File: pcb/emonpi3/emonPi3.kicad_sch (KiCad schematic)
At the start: 130 parts, among them CN1 CONN_03SCREW, CN2 CONN_03SCREW, CN3 CONN_03SCREW, J10 Conn_ARM_JTAG_SWD_10, J11 Conn_02x13_Odd_Even, J12 PINHD-1X9, J7 CONN_04PTH, J8 CONN_04PTH, J9 USB_C_Receptacle_USB2.0, SW1 SW_Push, SW2 SW_Push, SW3 SW_Push, U1 MCP1501-10xCH, U2 USBLC6-2P6, U3 ATSAMD21J17A-M, U4 AP2112K-3.3, U6 LMV331, U7 RFM69CW, U8 24AA02-OT

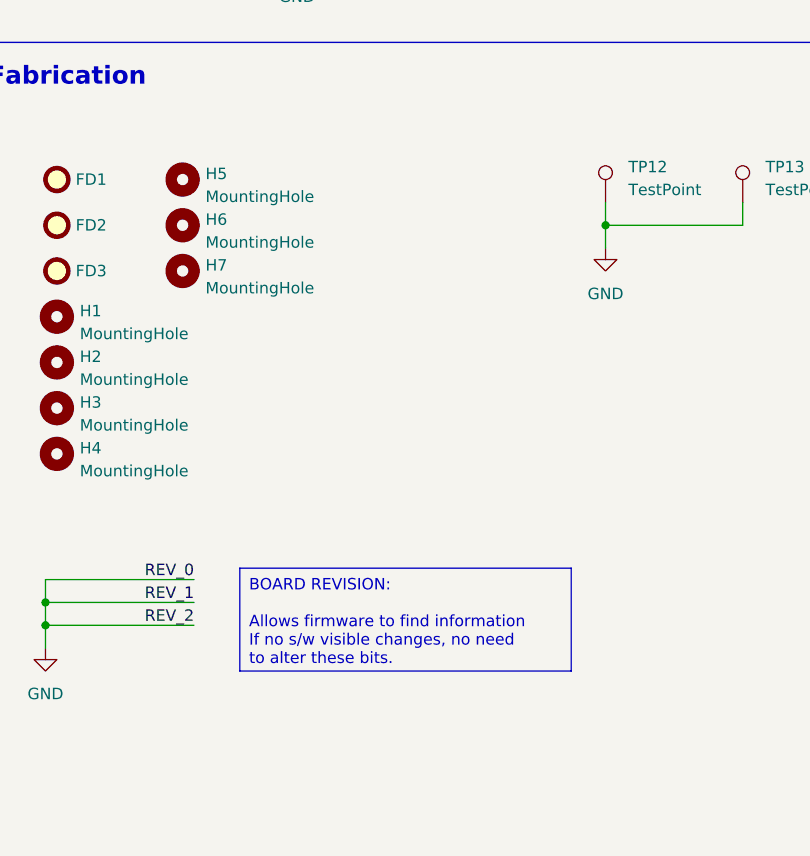
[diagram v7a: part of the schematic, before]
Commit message: * Add mounting hole for external WiFi board
  - 2.5 mm diameter for (future) WiFi extender
  - Move RST and IRQ from RFM, label 26pin header
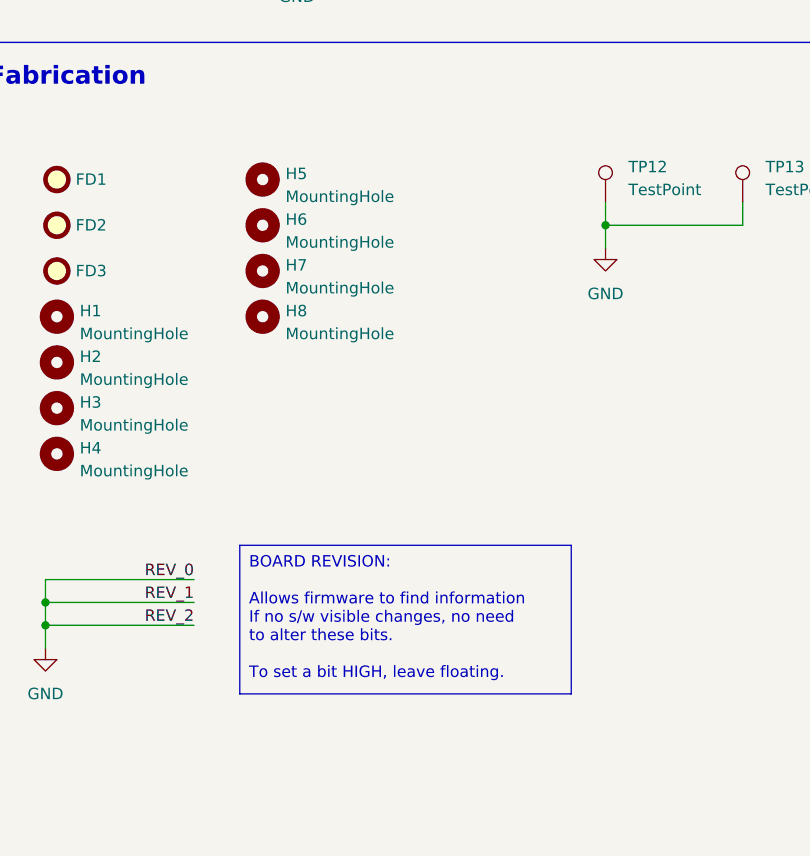
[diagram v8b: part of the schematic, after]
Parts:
- added H8: MountingHole, MountingHole:MountingHole_2.1mm, symbol Mechanical:MountingHole
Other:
- moved on the sheet: H5, H6, H7
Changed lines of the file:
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@@
     (effects (font (size 1.27 1.27)) (justify left top))
   )
-  (text_box "BOARD REVISION:\n\nAllows firmware to find information\nIf no s/w visible changes, no need\nto alter these bits."
-    (at 504.19 353.06 0) (size 36.83 11.43)
+  (text_box "BOARD REVISION:\n\nAllows firmware to find information\nIf no s/w visible changes, no need\nto alter these bits.\n\nTo set a bit HIGH, leave floating."
+    (at 504.19 350.52 0) (size 36.83 16.51)
     (stroke (width 0) (type default))
     (fill (type none))
@@
     )
   )
-  (symbol (lib_id "Mechanical:MountingHole") (at 497.84 320.04 0) (unit 1)
+  (symbol (lib_id "Mechanical:MountingHole") (at 506.73 320.04 0) (unit 1)
     (in_bom no) (on_board yes) (dnp no) (fields_autoplaced)
-    (property "Reference" "H7" (at 500.38 319.405 0)
+    (property "Reference" "H7" (at 509.27 319.405 0)
       (effects (font (size 1.27 1.27)) (justify left))
     )
-    (property "Value" "MountingHole" (at 500.38 321.945 0)
+    (property "Value" "MountingHole" (at 509.27 321.945 0)
       (effects (font (size 1.27 1.27)) (justify left))
     )
-    (property "Footprint" "MountingHole:MountingHole_2.1mm" (at 497.84 320.04 0)
+    (property "Footprint" "MountingHole:MountingHole_2.1mm" (at 506.73 320.04 0)
       (effects (font (size 1.27 1.27)) hide)
     )
-    (property "Datasheet" "~" (at 497.84 320.04 0)
+    (property "Datasheet" "~" (at 506.73 320.04 0)
       (effects (font (size 1.27 1.27)) hide)
     )
@@
     )
   )
-  (symbol (lib_id "Mechanical:MountingHole") (at 497.84 314.96 0) (unit 1)
+  (symbol (lib_id "Mechanical:MountingHole") (at 506.73 314.96 0) (unit 1)
     (in_bom no) (on_board yes) (dnp no) (fields_autoplaced)
-    (property "Reference" "H6" (at 500.38 314.325 0)
+    (property "Reference" "H6" (at 509.27 314.325 0)
       (effects (font (size 1.27 1.27)) (justify left))
     )
-    (property "Value" "MountingHole" (at 500.38 316.865 0)
+    (property "Value" "MountingHole" (at 509.27 316.865 0)
       (effects (font (size 1.27 1.27)) (justify left))
     )
-    (property "Footprint" "MountingHole:MountingHole_2.1mm" (at 497.84 314.96 0)
+    (property "Footprint" "MountingHole:MountingHole_2.1mm" (at 506.73 314.96 0)
       (effects (font (size 1.27 1.27)) hide)
     )
-    (property "Datasheet" "~" (at 497.84 314.96 0)
+    (property "Datasheet" "~" (at 506.73 314.96 0)
       (effects (font (size 1.27 1.27)) hide)
     )
@@
     )
   )
-  (symbol (lib_id "Mechanical:MountingHole") (at 497.84 309.88 0) (unit 1)
+  (symbol (lib_id "Mechanical:MountingHole") (at 506.73 309.88 0) (unit 1)
     (in_bom no) (on_board yes) (dnp no) (fields_autoplaced)
-    (property "Reference" "H5" (at 500.38 309.245 0)
+    (property "Reference" "H5" (at 509.27 309.245 0)
       (effects (font (size 1.27 1.27)) (justify left))
     )
-    (property "Value" "MountingHole" (at 500.38 311.785 0)
+    (property "Value" "MountingHole" (at 509.27 311.785 0)
       (effects (font (size 1.27 1.27)) (justify left))
     )
-    (property "Footprint" "MountingHole:MountingHole_2.1mm" (at 497.84 309.88 0)
+    (property "Footprint" "MountingHole:MountingHole_2.1mm" (at 506.73 309.88 0)
       (effects (font (size 1.27 1.27)) hide)
     )
-    (property "Datasheet" "~" (at 497.84 309.88 0)
+    (property "Datasheet" "~" (at 506.73 309.88 0)
       (effects (font (size 1.27 1.27)) hide)
     )
@@
         )
       )
+    )
+  )
+  (symbol (lib_id "Mechanical:MountingHole") (at 506.73 325.12 0) (unit 1)
+    (in_bom no) (on_board yes) (dnp no) (fields_autoplaced)
+    (property "Reference" "H8" (at 509.27 324.485 0)
+      (effects (font (size 1.27 1.27)) (justify left))
+    )
+    (property "Value" "MountingHole" (at 509.27 327.025 0)
+      (effects (font (size 1.27 1.27)) (justify left))
+    )
+    (property "Footprint" "MountingHole:MountingHole_2.1mm" (at 506.73 325.12 0)
+      (effects (font (size 1.27 1.27)) hide)
+    )
+    (property "Datasheet" "~" (at 506.73 325.12 0)
+      (effects (font (size 1.27 1.27)) hide)
+    )
+    (instances
+      (project "emonPi3"
+        (path "/3a5f1087-1abe-4575-9313-bd86a5e03366"
+          (reference "H8") (unit 1)
+        )
+      )
